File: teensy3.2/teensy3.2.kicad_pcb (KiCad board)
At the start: 4 copper layers, 70 x 25 mm, 80 parts, among them J2 USB_B_Micro, SW1 Prog, U1 LP38691SD-3.3, U2 MKL02Z32VFG4, U3 MK20DX256VLH7, Y1 32.768 KHz, Y2 16 MHz

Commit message: avances pcb
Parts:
- moved R1 90.4 mm to (95.0, 130.0), turned to 180 degrees
- moved R2 87.8 mm to (95.0, 128.5), turned to 180 degrees
- moved C1 84.5 mm to (91.2, 121.5), turned to 180 degrees
- moved Y2 84.4 mm to (129.0, 138.0)
- moved U2 82.0 mm to (103.0, 138.0), turned to 180 degrees
- moved SW1 75.5 mm to (93.9, 138.4), turned to 180 degrees
- moved TP10 74.9 mm to (85.0, 138.5)
- moved TP1 72.9 mm to (85.0, 145.5)
- moved D1 71.3 mm to (95.2, 121.8), turned to 180 degrees
- moved L2 70.5 mm to (108.5, 113.5)
- moved Y1 70.3 mm to (107.0, 129.0), turned to 90 degrees
- moved C4 67.9 mm to (94.5, 117.1), turned to 90 degrees
- moved C10 62.7 mm to (113.5, 118.2), turned to 90 degrees
- moved C5 62.3 mm to (116.2, 129.5)
- moved C6 61.6 mm to (138.5, 130.0), turned to 180 degrees
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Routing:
- net GND: track 0.00 -> 1.22 mm
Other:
- board size 70 x 25 mm -> 63.5 x 42.5 mm
- copper layers 4 -> 2

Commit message: avances sch + pcb
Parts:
- removed TP1: VBAT, TestPoint:TestPoint_THTPad_D2.0mm_Drill1.0mm
- removed TP10: PROG, TestPoint:TestPoint_THTPad_D2.0mm_Drill1.0mm
- removed TP11: AGND, TestPoint:TestPoint_THTPad_D2.0mm_Drill1.0mm
- removed TP12: AREF, TestPoint:TestPoint_THTPad_D2.0mm_Drill1.0mm
- removed TP13: RESET, TestPoint:TestPoint_THTPad_D2.0mm_Drill1.0mm
- removed TP14: 31, TestPoint:TestPoint_THTPad_D2.0mm_Drill1.0mm
- removed TP15: 26, TestPoint:TestPoint_THTPad_D2.0mm_Drill1.0mm
- removed TP16: A10, TestPoint:TestPoint_THTPad_D2.0mm_Drill1.0mm
- removed TP17: A11, TestPoint:TestPoint_THTPad_D2.0mm_Drill1.0mm
- removed TP18: A12, TestPoint:TestPoint_THTPad_D2.0mm_Drill1.0mm
- removed TP19: A13, TestPoint:TestPoint_THTPad_D2.0mm_Drill1.0mm
- removed TP2: VUSB, TestPoint:TestPoint_THTPad_D2.0mm_Drill1.0mm
- removed TP20: 33, TestPoint:TestPoint_THTPad_D2.0mm_Drill1.0mm
- removed TP21: 24, TestPoint:TestPoint_THTPad_D2.0mm_Drill1.0mm
- removed TP22: 3, TestPoint:TestPoint_THTPad_D2.0mm_Drill1.0mm
- removed TP23: 4, TestPoint:TestPoint_THTPad_D2.0mm_Drill1.0mm
- removed TP24: DAC/A14, TestPoint:TestPoint_THTPad_D2.0mm_Drill1.0mm
- removed TP25: 16/A2, TestPoint:TestPoint_THTPad_D2.0mm_Drill1.0mm
- removed TP26: 17/A3, TestPoint:TestPoint_THTPad_D2.0mm_Drill1.0mm
- removed TP27: 19/A5, TestPoint:TestPoint_THTPad_D2.0mm_Drill1.0mm
- removed TP28: 18/A4, TestPoint:TestPoint_THTPad_D2.0mm_Drill1.0mm
- removed TP29: 0, TestPoint:TestPoint_THTPad_D2.0mm_Drill1.0mm
- removed TP3, TP4, TP6: 3.3V, TestPoint:TestPoint_THTPad_D2.0mm_Drill1.0mm
- removed TP30: 1, TestPoint:TestPoint_THTPad_D2.0mm_Drill1.0mm
- removed TP31: 32, TestPoint:TestPoint_THTPad_D2.0mm_Drill1.0mm
- removed TP32: 25, TestPoint:TestPoint_THTPad_D2.0mm_Drill1.0mm
- removed TP33: 15/A1, TestPoint:TestPoint_THTPad_D2.0mm_Drill1.0mm
- removed TP34: 22/A8, TestPoint:TestPoint_THTPad_D2.0mm_Drill1.0mm
- removed TP35: 23/A9, TestPoint:TestPoint_THTPad_D2.0mm_Drill1.0mm
- removed TP36: 9, TestPoint:TestPoint_THTPad_D2.0mm_Drill1.0mm
- removed TP37: 10, TestPoint:TestPoint_THTPad_D2.0mm_Drill1.0mm
- removed TP38: 11, TestPoint:TestPoint_THTPad_D2.0mm_Drill1.0mm
- removed TP39: 12, TestPoint:TestPoint_THTPad_D2.0mm_Drill1.0mm
- removed TP40: 28, TestPoint:TestPoint_THTPad_D2.0mm_Drill1.0mm
- removed TP41: 27, TestPoint:TestPoint_THTPad_D2.0mm_Drill1.0mm
- removed TP42: 29, TestPoint:TestPoint_THTPad_D2.0mm_Drill1.0mm
- removed TP43: 30, TestPoint:TestPoint_THTPad_D2.0mm_Drill1.0mm
- removed TP44: 2, TestPoint:TestPoint_THTPad_D2.0mm_Drill1.0mm
- removed TP45: 14/A0, TestPoint:TestPoint_THTPad_D2.0mm_Drill1.0mm
- removed TP46: 7, TestPoint:TestPoint_THTPad_D2.0mm_Drill1.0mm
- removed TP47: 8, TestPoint:TestPoint_THTPad_D2.0mm_Drill1.0mm
- removed TP48: 6, TestPoint:TestPoint_THTPad_D2.0mm_Drill1.0mm
- removed TP49: 20/A6, TestPoint:TestPoint_THTPad_D2.0mm_Drill1.0mm
- removed TP5: VIN, TestPoint:TestPoint_THTPad_D2.0mm_Drill1.0mm
- removed TP50: 21/A7, TestPoint:TestPoint_THTPad_D2.0mm_Drill1.0mm
- removed TP51: 5, TestPoint:TestPoint_THTPad_D2.0mm_Drill1.0mm
- removed TP52: 13 (LED), TestPoint:TestPoint_THTPad_D2.0mm_Drill1.0mm
- removed TP7, TP8, TP9: GND, TestPoint:TestPoint_THTPad_D2.0mm_Drill1.0mm
- added FID1: Fiducial, Fiducial:Fiducial_0.5mm_Mask1.5mm, F.Cu at (135.0, 106.0)
- added J1: USB_B_Micro, Connector_USB:USB_Micro-B_Molex_47346-0001, F.Cu at (103.0, 93.0)
- added J3: Conn_01x26, Connector_PinSocket_2.54mm:PinSocket_1x26_P2.54mm_Vertical, F.Cu at (103.0, 112.0)
- C1, C10, C11, C5, C6, C7: footprint Capacitor_SMD:C_0603_1608Metric -> Capacitor_SMD:C_0805_2012Metric
- C8: value 2.2uF -> 0.1uF
- J2: value USB_B_Micro -> Conn_01x26; footprint Connector_USB:USB_Micro-B_Molex_47346-0001 -> Connector_PinSocket_2.54mm:PinSocket_1x26_P2.54mm_Vertical
- L1, L2: footprint Inductor_SMD:L_0201_0603Metric -> Inductor_SMD:L_0805_2012Metric
- R1, R2, R3, R4: footprint Resistor_SMD:R_0201_0603Metric -> Resistor_SMD:R_0805_2012Metric
- Y1: footprint Crystal:Crystal_SMD_TXC_AX_8045-2Pin_8.0x4.5mm -> Crystal:Crystal_SMD_2012-2Pin_2.0x1.2mm
- Y2: footprint Crystal:Crystal_SMD_HC49-SD -> Crystal:Crystal_SMD_2016-4Pin_2.0x1.6mm
- moved J2 56.2 mm to (102.5, 72.5), turned to 90 degrees
- moved SW1 56.0 mm to (124.5, 91.5)
- moved R3 45.4 mm to (128.5, 79.0), turned to 270 degrees
- moved U2 44.3 mm to (123.0, 98.5)
- moved R2 44.1 mm to (114.5, 89.0)
- moved R1 43.2 mm to (114.5, 91.5)
- moved C6 43.0 mm to (154.5, 90.1), turned to 270 degrees
- moved Y1 42.9 mm to (135.0, 96.5), turned to 270 degrees
- moved C11 42.2 mm to (128.5, 83.5)
- moved C9 40.5 mm to (125.0, 79.0), turned to 270 degrees
- moved R4 40.3 mm to (155.6, 81.0)
- moved C1 39.2 mm to (127.0, 105.6), turned to 90 degrees
- moved L1 38.7 mm to (121.5, 79.0), turned to 270 degrees
- moved Y2 37.0 mm to (144.7, 104.5)
- moved C10 36.6 mm to (125.0, 83.5), turned to 270 degrees
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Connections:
- net Net-(C3-Pad1) renamed /VIN
- net Net-(SW1-Pad1) renamed /PROG
- net PTA0 renamed Net-(U2-Pad8)
- net PTA2 renamed Net-(U2-Pad9)
- net PTA3 renamed /PTA3
- net RESET renamed /RESET
- net USB0_DM renamed /USB0_DM
- net USB0_DP renamed /USB0_DP
- net VBAT renamed /U3_VBAT
- C10 pad 1: Net-(C10-Pad1) -> /AREF
- C10 pad 2: GNDA -> /AGND
- C11 pad 2: GNDA -> /AGND
- C9 pad 1: Net-(C9-Pad1) -> VDDA
- D1 pad 1: Net-(D1-Pad1) -> +3V3
- D1 pad 2: +3V3 -> /J3_VBAT
- D2 pad 2: Net-(D2-Pad2) -> /13
- F1 pad 1: Net-(F1-Pad1) -> Net-(C2-Pad1)
- F1 pad 2: Net-(C2-Pad1) -> /VUSB
- J2 pad 1: Net-(C2-Pad1) -> GND
- J2 pad 2: Net-(J2-Pad2) -> +3V3
- J2 pad 3: Net-(J2-Pad3) -> /AGND
- J2 pad 4: PTA1 -> /AREF
- J2 pad 5: GND -> /A13
- J2 pad 6: GND -> /A12
- JP1 pad 1: Net-(F1-Pad1) -> /VUSB
- L1 pad 2: Net-(C9-Pad1) -> VDDA
- R1 pad 2: Net-(J2-Pad3) -> Net-(J1-Pad3)
- R2 pad 2: Net-(J2-Pad2) -> Net-(J1-Pad2)
- R3 pad 1: Net-(C10-Pad1) -> VDDA
- R3 pad 2: Net-(C9-Pad1) -> /AREF
- U2 pad 6: PTA1 -> /PTA1
- U3 pad 1: Net-(TP14-Pad1) -> /31
- U3 pad 10: Net-(TP17-Pad1) -> /A11
- U3 pad 11: Net-(TP18-Pad1) -> /A12
- U3 pad 12: Net-(TP19-Pad1) -> /A13
- U3 pad 13: Net-(C9-Pad1) -> VDDA
- U3 pad 14: Net-(C10-Pad1) -> /AREF
- U3 pad 15: GNDA -> /AGND
- U3 pad 16: GNDA -> /AGND
- U3 pad 18: Net-(TP24-Pad1) -> /DAC-A14
- U3 pad 2: Net-(TP15-Pad1) -> /26
- U3 pad 23: PTA1 -> /PTA1
- U3 pad 26: Net-(TP20-Pad1) -> /33
- U3 pad 27: Net-(TP21-Pad1) -> /24
- U3 pad 28: Net-(TP22-Pad1) -> /3
- U3 pad 29: Net-(TP23-Pad1) -> /4
- U3 pad 35: Net-(TP25-Pad1) -> /16-A2
- U3 pad 36: Net-(TP26-Pad1) -> /17-A3
- U3 pad 37: Net-(TP27-Pad1) -> /19-A5
- U3 pad 38: Net-(TP28-Pad1) -> /18-A4
- U3 pad 39: Net-(TP29-Pad1) -> /0
- U3 pad 40: Net-(TP30-Pad1) -> /1
- U3 pad 41: Net-(TP31-Pad1) -> /32
- U3 pad 42: Net-(TP32-Pad1) -> /25
- U3 pad 43: Net-(TP33-Pad1) -> /15-A1
- U3 pad 44: Net-(TP34-Pad1) -> /22-A8
- U3 pad 45: Net-(TP35-Pad1) -> /23-A9
- U3 pad 46: Net-(TP36-Pad1) -> /9
- U3 pad 49: Net-(TP37-Pad1) -> /10
- U3 pad 50: Net-(D2-Pad2) -> /13
- U3 pad 51: Net-(TP38-Pad1) -> /11
- U3 pad 52: Net-(TP39-Pad1) -> /12
- U3 pad 53: Net-(TP40-Pad1) -> /28
- U3 pad 54: Net-(TP41-Pad1) -> /27
- U3 pad 55: Net-(TP42-Pad1) -> /29
- U3 pad 56: Net-(TP43-Pad1) -> /30
- U3 pad 57: Net-(TP44-Pad1) -> /2
- U3 pad 58: Net-(TP45-Pad1) -> /14-A0
- U3 pad 59: Net-(TP46-Pad1) -> /7
- U3 pad 60: Net-(TP47-Pad1) -> /8
- U3 pad 61: Net-(TP48-Pad1) -> /6
- U3 pad 62: Net-(TP49-Pad1) -> /20-A6
- U3 pad 63: Net-(TP50-Pad1) -> /21-A7
- U3 pad 64: Net-(TP51-Pad1) -> /5
- U3 pad 9: Net-(TP16-Pad1) -> /A10
- Y1 pad 1: Net-(U3-Pad20) -> Net-(U3-Pad19)
- Y1 pad 2: Net-(U3-Pad19) -> Net-(U3-Pad20)
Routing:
- net GND: track 1.22 -> 0.00 mm
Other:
- board outline removed
- net class Default: clearance 0.127 -> 0.18; trace_width 0.127 -> 0.2; via_dia 0.457 -> 0.8; via_drill 0.3 -> 0.4
- rule trace_clearance: 0.127 -> 0.18

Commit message: avances pcb
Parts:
- moved FID1 30.1 mm to (165.0, 103.0)
- moved C8 25.9 mm to (160.0, 93.5), turned to 270 degrees
- moved C9 14.5 mm to (114.6, 89.0), turned to 180 degrees
- moved L1 13.9 mm to (109.4, 86.0), turned to 0 degrees
- moved C7 13.6 mm to (142.5, 86.0)
- moved C6 13.5 mm to (150.5, 103.0), turned to 0 degrees
- moved L2 13.2 mm to (109.5, 89.0), turned to 180 degrees
- moved R4 11.7 mm to (164.6, 88.5)
- moved R3 11.4 mm to (119.6, 86.0), turned to 180 degrees
- moved C10 10.8 mm to (114.5, 86.0), turned to 180 degrees
- moved C11 10.5 mm to (119.5, 89.0), turned to 180 degrees
- moved D2 9.19 mm to (164.6, 85.5)
- moved J2 7.00 mm to (102.5, 79.5)
- moved U3 5.83 mm to (149.5, 93.0)
- moved C3 5.05 mm to (103.0, 102.0)
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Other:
- board text added: "Mínimos (Mayer 8 mils): Grillas: 0. 5mm, 0.25 mm Vía: 0.8 mm (0.4 mm) Margen: 0.18 mm Pista: 0.20 mm Dist. a borde: 0.30 mm Terminación: HASL"

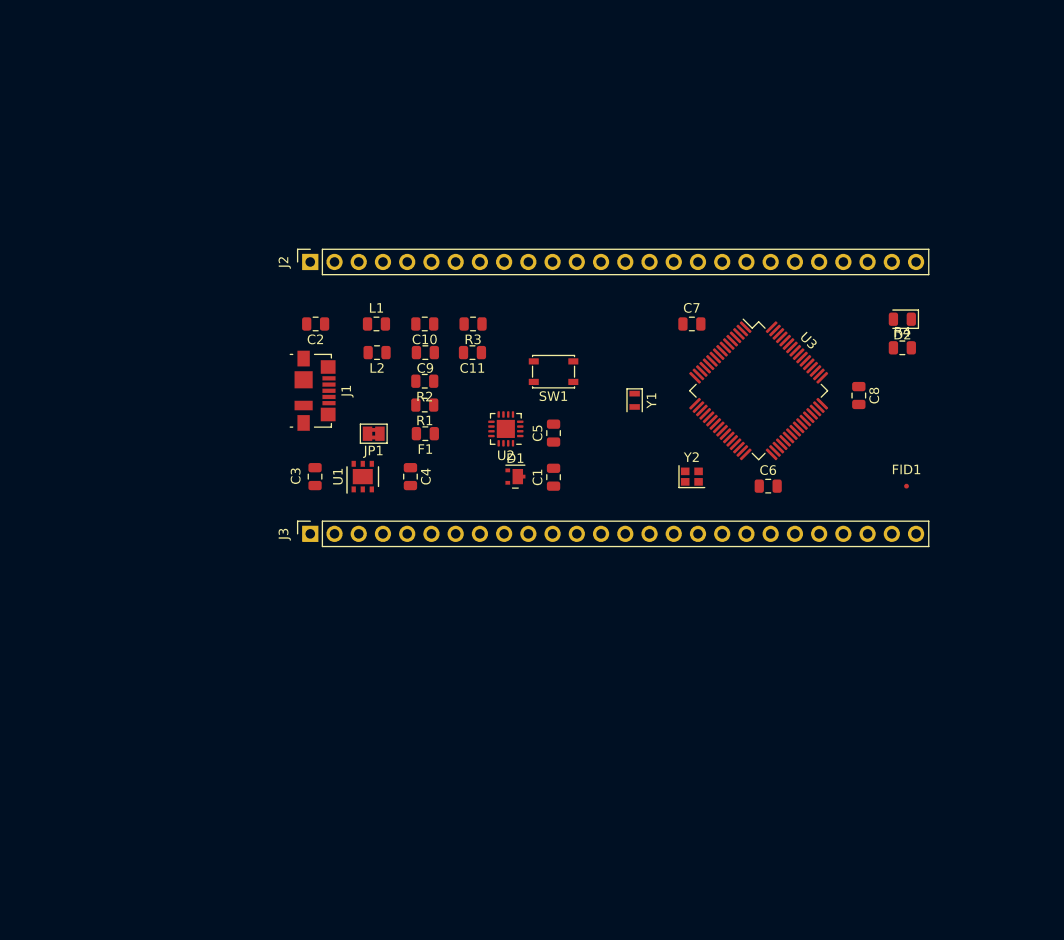
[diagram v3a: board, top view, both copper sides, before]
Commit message: avances ruteo pcb
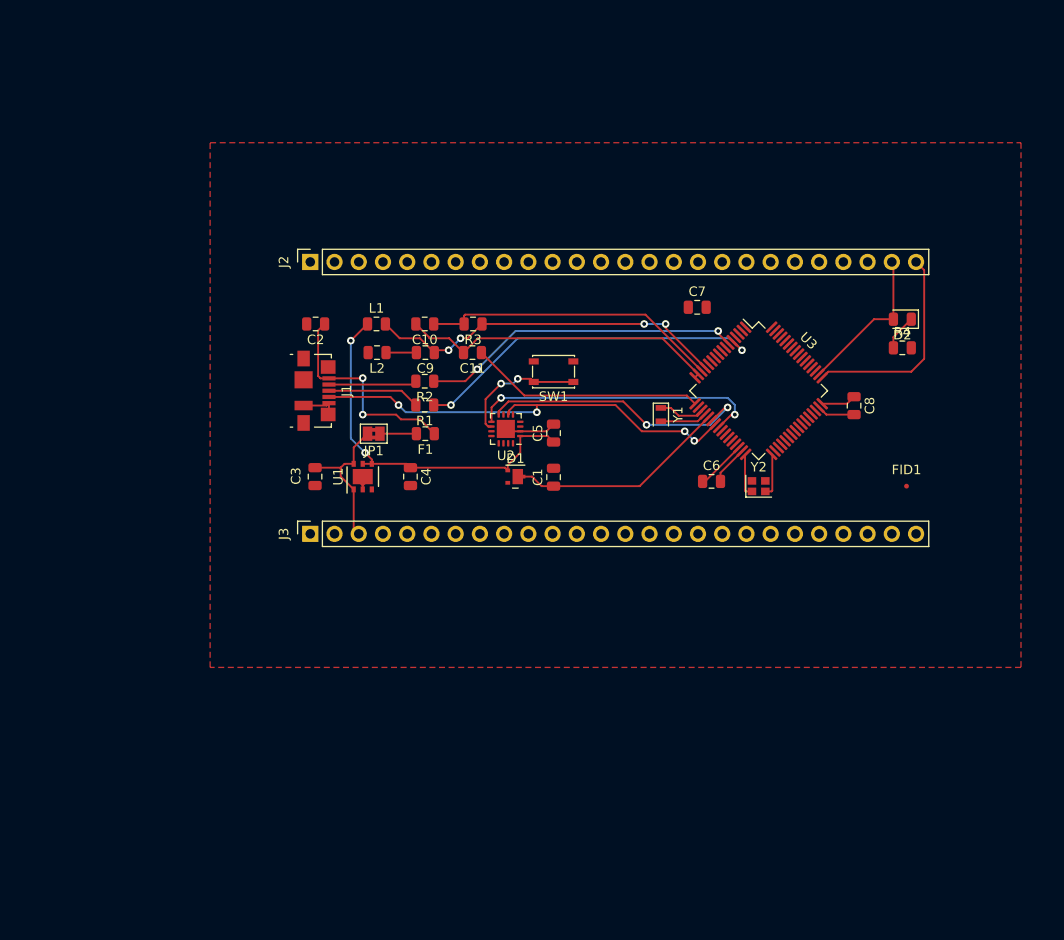
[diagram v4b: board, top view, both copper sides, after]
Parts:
- moved Y2 7.07 mm to (149.5, 103.0)
- moved C6 5.96 mm to (144.6, 102.5)
- moved Y1 3.13 mm to (139.2, 95.5)
- moved C7 1.84 mm to (143.1, 84.2)
- moved C8 1.17 mm to (159.5, 94.6)
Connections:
- net /0 renamed Net-(J3-Pad19)
- net /1 renamed Net-(J3-Pad20)
- net /10 renamed Net-(J2-Pad26)
- net /11 renamed Net-(J2-Pad24)
- net /12 renamed Net-(J2-Pad23)
- net /13 renamed /LED
- net /14-A0 renamed Net-(J2-Pad17)
- net /15-A1 renamed Net-(J3-Pad23)
- net /16-A2 renamed Net-(J3-Pad15)
- net /17-A3 renamed Net-(J3-Pad16)
- net /18-A4 renamed Net-(J3-Pad18)
- net /19-A5 renamed Net-(J3-Pad17)
- net /2 renamed Net-(J2-Pad18)
- net /20-A6 renamed Net-(J2-Pad13)
- net /21-A7 renamed Net-(J2-Pad12)
- net /22-A8 renamed Net-(J3-Pad24)
- net /23-A9 renamed Net-(J3-Pad25)
- net /24 renamed /J2_12
- net /25 renamed Net-(J3-Pad22)
- net /26 renamed /J2_9
- net /27 renamed Net-(J2-Pad21)
- net /28 renamed Net-(J2-Pad22)
- net /29 renamed Net-(J2-Pad20)
- net /3 renamed /J2_13
- net /30 renamed Net-(J2-Pad19)
- net /31 renamed /J2_10
- net /32 renamed Net-(J3-Pad21)
- net /33 renamed /J2_11
- net /4 renamed /J2_14
- net /5 renamed Net-(J2-Pad11)
- net /6 renamed Net-(J2-Pad14)
- net /7 renamed Net-(J2-Pad16)
- net /8 renamed Net-(J2-Pad15)
- net /9 renamed Net-(J3-Pad26)
- net /A10 renamed /J2_8
- net /A11 renamed /J2_7
- net /A12 renamed /J2_6
- net /A13 renamed /J2_5
- net /DAC-A14 renamed Net-(J3-Pad10)
- net /J3_VBAT renamed Net-(D1-Pad2)
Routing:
- net +3V3: track 0.00 -> 48.6 mm, vias 0 -> 2
- net /PTA1: track 0.00 -> 47.8 mm, vias 0 -> 4
- net VDDA: track 0.00 -> 38.2 mm, vias 0 -> 4
- net /USB0_DP: track 0.00 -> 37.2 mm, vias 0 -> 2
- net /USB0_DM: track 0.00 -> 33.8 mm, vias 0 -> 2
- net /AGND: track 0.00 -> 33.6 mm
- net /AREF: track 0.00 -> 31.5 mm
- net Net-(U2-Pad9): track 0.00 -> 31.0 mm, vias 0 -> 2
- net Net-(U2-Pad8): track 0.00 -> 28.8 mm, vias 0 -> 2
- net Net-(C11-Pad1): track 0.00 -> 24.6 mm
- net /U3_VBAT: track 0.00 -> 23.4 mm
- net Net-(C2-Pad1): track 0.00 -> 22.7 mm, vias 0 -> 2
- net Net-(J2-Pad26): track 0.00 -> 22.0 mm
- net GND: track 0.00 -> 21.1 mm
- net /LED: track 0.00 -> 16.3 mm
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- added copper zone on F.Cu, net GND

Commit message: fin ruteo pcb
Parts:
- moved FID1 3.64 mm to (166.0, 99.5)
- moved U2 1.03 mm to (123.2, 98.0)
- moved C5 0.12 mm to (128.0, 97.6)
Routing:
- net +3V3: track 48.6 -> 129.7 mm, vias 2 -> 8
- net /RESET: track 0.00 -> 56.4 mm, vias 0 -> 3
- net GND: track 21.1 -> 67.6 mm, vias 0 -> 8
- net /J2_5: track 0.00 -> 37.1 mm
- net /J2_6: track 0.00 -> 33.9 mm
- net /J2_7: track 0.00 -> 31.5 mm
- net /PTA3: track 0.00 -> 29.3 mm, vias 0 -> 2
- net /J2_8: track 0.00 -> 29.2 mm, vias 0 -> 1
- net /J2_9: track 0.00 -> 27.9 mm, vias 0 -> 1
- net Net-(J2-Pad11): track 0.00 -> 25.8 mm
- net /J2_10: track 0.00 -> 25.7 mm, vias 0 -> 1
- net Net-(J2-Pad12): track 0.00 -> 25.1 mm
- net Net-(J3-Pad10): track 0.00 -> 23.6 mm, vias 0 -> 1
- net Net-(J2-Pad13): track 0.00 -> 23.4 mm
- net /J2_11: track 0.00 -> 22.4 mm, vias 0 -> 1
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- added copper zone on B.Cu, net GND
